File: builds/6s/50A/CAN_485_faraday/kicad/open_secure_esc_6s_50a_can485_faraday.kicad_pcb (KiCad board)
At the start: 4 copper layers, 32 x 66.1 mm, 59 parts, among them J1 SolderPad_1x04_SMD_P1.27mm_Pr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, J2 SolderPad_1x02_SMD_P2.54mm, J3 SolderPad_1x02_SMD_P2.54mm, J4A SolderWirePad_1x01_SMD_5x10mm, J4B SolderWirePad_1x01_SMD_5x10mm, J4C SolderWirePad_1x01_SMD_5x10mm, J5A SolderWire-6sqmm_1x01_D3.5mm_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, J5B SolderWire-6sqmm_1x01_D3.5mm_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, Q1 Toshiba_2-5W1A_SOP-Advance-N_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, Q2 Toshiba_2-5W1A_SOP-Advance-N_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, Q3 Toshiba_2-5W1A_SOP-Advance-N_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, Q4 Toshiba_2-5W1A_SOP-Advance-N_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, Q5 Toshiba_2-5W1A_SOP-Advance-N_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, Q6 Toshiba_2-5W1A_SOP-Advance-N_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, U1 LQFP-64_10x10mm_P0.5mm, U2 Infineon_PG-USON-10-2-4_3x3mm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, U3 SOIC-20W_7.5x12.8mm_P1.27mm, U4 SOIC-20W_7.5x12.8mm_P1.27mm, U5 TI_RTA0040B_WQFN-40_6x6mm_P0.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, U6 SOIC-8_3.9x4.9mm_P1.27mm, U7 SOIC-8_3.9x4.9mm_P1.27mm, U8 SOIC-8_3.9x4.9mm_P1.27mm

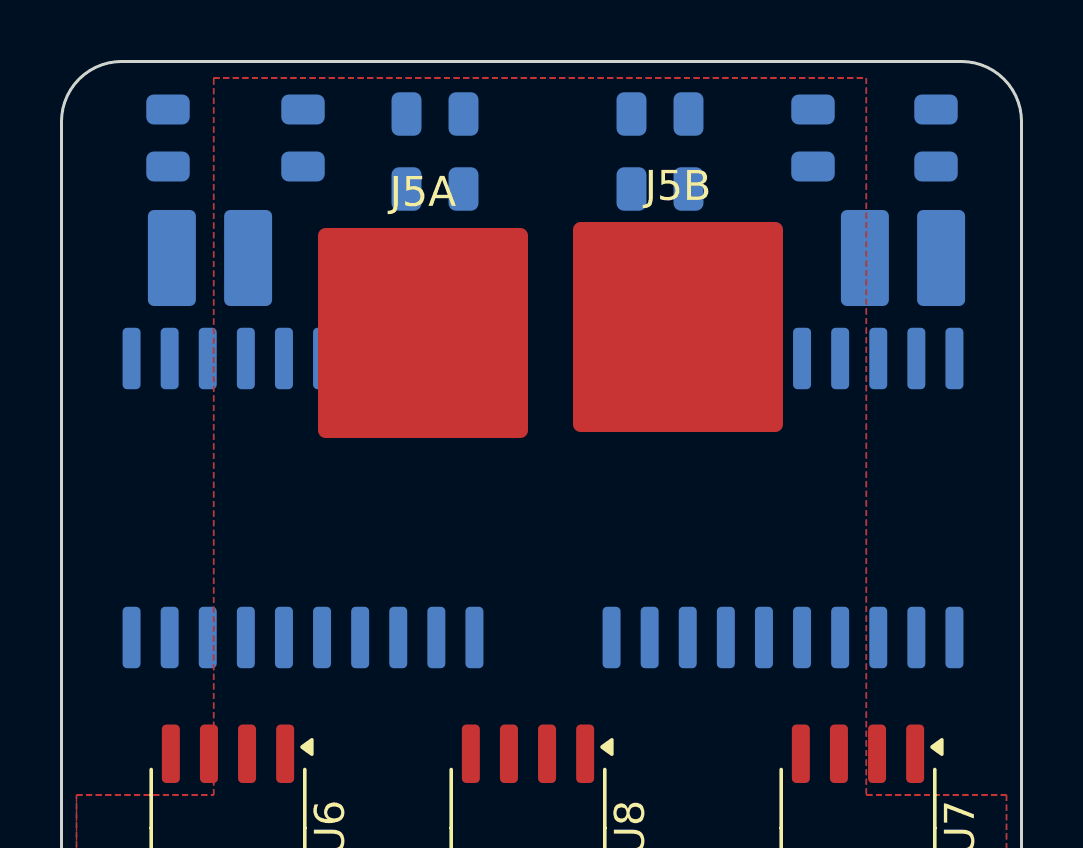
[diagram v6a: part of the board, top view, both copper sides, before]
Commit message: Score connectivity too: the +/-1.0 mm spread was breaking GND
Correcting the previous commit rather than leaving it standing. It applied a
+/-1.0 mm transceiver spread and reported "DRC electrical 0". The DRC number
was real; the conclusion drawn from it was not.

score_placement.py read only kicad-cli's "violations" array. kicad-cli reports
broken connections in a SEPARATE "unconnected_items" array, so the harness was
structurally blind to them. Checking by hand:

    before the spread   159 unconnected
    after  the spread   161 unconnected

The +/-1.0 mm move severed two GND connections. Refilling the pour around the
displaced parts fragments the B.Cu GND pour, and two of the eight newly
unconnected items belong to U5 -- a part that never moved. Gaining creepage by
cutting a ground connection is not a gain.

Re-swept with connectivity scored:

    spread   creepage   DRC-el   unconnected
    +/-0.00    7.51        0         159
    +/-0.25    7.66        0         159
    +/-0.50    7.83        0         159   <- applied
    +/-0.75    7.98        0         160
    +/-1.00    7.98        0         161

Backed off to +/-0.5 mm: creepage 7.51 -> 7.83 (0.33 mm margin, not the 0.48
previously claimed), isolated lead unchanged at 9.76 mm, both isolation rules
still passing, and no net broken. The extra 0.15 mm is available later if GND
stitching is done deliberately.

drc_electrical() now returns (violations, unconnected) and the report prints
the second with a BROKEN NETS marker. The 159 baseline is pre-existing and
largely unrouted copper, not damage from this work -- it is now visible on
every run instead of invisible on all of them.

Fourth harness defect found by checking output against geometry, and the first
one where the harness was not wrong about what it measured but silent about
what it did not.

Co-Authored-By: Claude Opus 5 <noreply@anthropic.com>
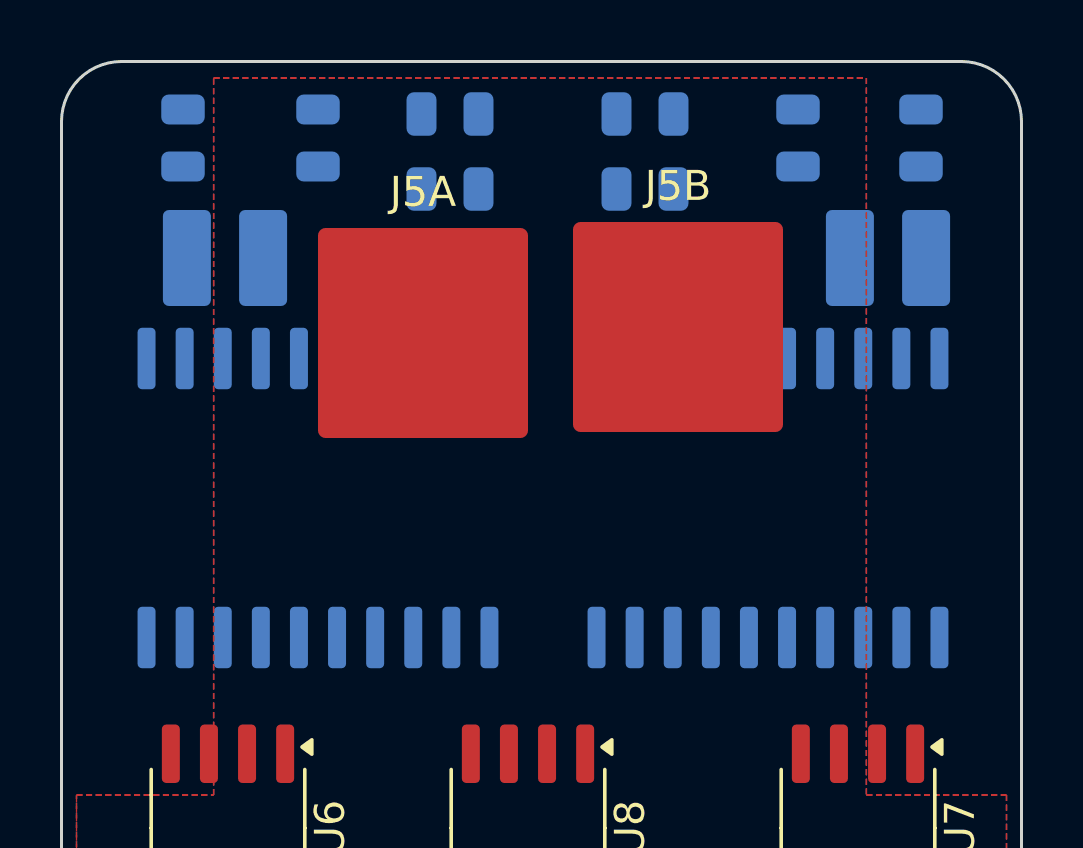
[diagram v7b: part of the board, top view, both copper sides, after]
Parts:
- moved C11 0.50 mm to (32.9, 21.7)
- moved C12 0.50 mm to (32.9, 24.2)
- moved C13 0.50 mm to (28.5, 22.5)
- moved C14 0.50 mm to (24.0, 22.5)
- moved C15 0.50 mm to (39.4, 21.7)
- moved C16 0.50 mm to (39.4, 24.2)
- moved C17 0.50 mm to (44.5, 22.5)
- moved C18 0.50 mm to (48.6, 22.5)
- moved FB1 0.50 mm to (32.4, 26.5)
- moved FB2 0.50 mm to (29.9, 26.5)
- moved FB3 0.50 mm to (39.4, 26.5)
- moved FB4 0.50 mm to (41.9, 26.5)
- moved J2 0.50 mm to (25.4, 26.5)
- moved J3 0.50 mm to (47.5, 26.5)
- moved U3 0.50 mm to (28.5, 34.5)
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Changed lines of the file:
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@@
 	(footprint "C_0805_2012Metric"
 		(layer "B.Cu")
-		(at 28 22.5 -90)
+		(at 28.5 22.5 -90)
 		(descr "Capacitor SMD 0805 (2012 Metric), square (rectangular) end terminal, IPC-7351 nominal, (Body size source: IPC-SM-782 page 76, https://www.pcb-3d.com/wordpress/wp-content/uploads/ipc-sm-782a_amendment_1_and_2.pdf, https://docs.google.com/spreadsheets/d/1BsfQQcO9C6DZCsRaXUlFlo91Tg2WpOkGARC1WS5S8t0/edit?usp=sharing), generated with kicad-footprint-generator")
 		(tags "capacitor")
@@
 	(footprint "C_0805_2012Metric"
 		(layer "B.Cu")
-		(at 32.4 21.7)
+		(at 32.9 21.7)
 		(descr "Capacitor SMD 0805 (2012 Metric), square (rectangular) end terminal, IPC-7351 nominal, (Body size source: IPC-SM-782 page 76, https://www.pcb-3d.com/wordpress/wp-content/uploads/ipc-sm-782a_amendment_1_and_2.pdf, https://docs.google.com/spreadsheets/d/1BsfQQcO9C6DZCsRaXUlFlo91Tg2WpOkGARC1WS5S8t0/edit?usp=sharing), generated with kicad-footprint-generator")
 		(tags "capacitor")
@@
 	(footprint "L_0402_1005Metric"
 		(layer "B.Cu")
-		(at 39.9 26.5)
+		(at 39.4 26.5)
 		(descr "Inductor SMD 0402 (1005 Metric), square (rectangular) end terminal, IPC-7351 nominal, (Body size source: http://www.tortai-tech.com/upload/download/2011102023233369053.pdf), generated with kicad-footprint-generator")
 		(tags "inductor")
@@
 	(footprint "SolderPad_1x02_SMD_P2.54mm"
 		(layer "B.Cu")
-		(at 24.9 26.5)
+		(at 25.4 26.5)
 		(descr "Bare SMD solder-pad strip, 2 pads, 2.54 mm pitch, 1.6 x 3.2 mm pads. Replaces a through-hole pin header so the opposite board side stays usable -- see symbols/tools/gen_smd_solder_pad_footprints.py. No connector body, no retention, no mating part: a wire solders directly to the pad. Pad geometry is an ENGINEERING DEFAULT (AGENTS.md Sec.4), not a datasheet or IPC value. Precedent: Vimdrones ESC S50 [47] 'CAN Port Connector: Solder PAD'.")
 		(tags "solder pad SMD wire connector 1x02 2.54mm")
@@
 	(footprint "SOIC-20W_7.5x12.8mm_P1.27mm"
 		(layer "B.Cu")
-		(at 44 34.5 90)
+		(at 43.5 34.5 90)
 		(descr "SOIC, 20 Pin (JEDEC MS-013AC, https://www.analog.com/media/en/package-pcb-resources/package/233848rw_20.pdf), generated with kicad-footprint-generator ipc_gullwing_generator.py")
 		(tags "SOIC SO")
@@
 	(footprint "C_0805_2012Metric"
 		(layer "B.Cu")
-		(at 39.9 21.7)
+		(at 39.4 21.7)
 		(descr "Capacitor SMD 0805 (2012 Metric), square (rectangular) end terminal, IPC-7351 nominal, (Body size source: IPC-SM-782 page 76, https://www.pcb-3d.com/wordpress/wp-content/uploads/ipc-sm-782a_amendment_1_and_2.pdf, https://docs.google.com/spreadsheets/d/1BsfQQcO9C6DZCsRaXUlFlo91Tg2WpOkGARC1WS5S8t0/edit?usp=sharing), generated with kicad-footprint-generator")
 		(tags "capacitor")
@@
 	(footprint "SOIC-20W_7.5x12.8mm_P1.27mm"
 		(layer "B.Cu")
-		(at 28 34.5 90)
+		(at 28.5 34.5 90)
 		(descr "SOIC, 20 Pin (JEDEC MS-013AC, https://www.analog.com/media/en/package-pcb-resources/package/233848rw_20.pdf), generated with kicad-footprint-generator ipc_gullwing_generator.py")
 		(tags "SOIC SO")
@@
 	(footprint "C_0805_2012Metric"
 		(layer "B.Cu")
-		(at 45 22.5 -90)
+		(at 44.5 22.5 -90)
 		(descr "Capacitor SMD 0805 (2012 Metric), square (rectangular) end terminal, IPC-7351 nominal, (Body size source: IPC-SM-782 page 76, https://www.pcb-3d.com/wordpress/wp-content/uploads/ipc-sm-782a_amendment_1_and_2.pdf, https://docs.google.com/spreadsheets/d/1BsfQQcO9C6DZCsRaXUlFlo91Tg2WpOkGARC1WS5S8t0/edit?usp=sharing), generated with kicad-footprint-generator")
 		(tags "capacitor")
@@
 	(footprint "L_0402_1005Metric"
 		(layer "B.Cu")
-		(at 29.4 26.5)
+		(at 29.9 26.5)
 		(descr "Inductor SMD 0402 (1005 Metric), square (rectangular) end terminal, IPC-7351 nominal, (Body size source: http://www.tortai-tech.com/upload/download/2011102023233369053.pdf), generated with kicad-footprint-generator")
 		(tags "inductor")
@@
 	(footprint "C_0805_2012Metric"
 		(layer "B.Cu")
-		(at 32.4 24.2)
+		(at 32.9 24.2)
 		(descr "Capacitor SMD 0805 (2012 Metric), square (rectangular) end terminal, IPC-7351 nominal, (Body size source: IPC-SM-782 page 76, https://www.pcb-3d.com/wordpress/wp-content/uploads/ipc-sm-782a_amendment_1_and_2.pdf, https://docs.google.com/spreadsheets/d/1BsfQQcO9C6DZCsRaXUlFlo91Tg2WpOkGARC1WS5S8t0/edit?usp=sharing), generated with kicad-footprint-generator")
 		(tags "capacitor")
@@
 	(footprint "L_0402_1005Metric"
 		(layer "B.Cu")
-		(at 42.4 26.5)
+		(at 41.9 26.5)
 		(descr "Inductor SMD 0402 (1005 Metric), square (rectangular) end terminal, IPC-7351 nominal, (Body size source: http://www.tortai-tech.com/upload/download/2011102023233369053.pdf), generated with kicad-footprint-generator")
 		(tags "inductor")
@@
 	(footprint "C_0805_2012Metric"
 		(layer "B.Cu")
-		(at 23.5 22.5 -90)
+		(at 24 22.5 -90)
 		(descr "Capacitor SMD 0805 (2012 Metric), square (rectangular) end terminal, IPC-7351 nominal, (Body size source: IPC-SM-782 page 76, https://www.pcb-3d.com/wordpress/wp-content/uploads/ipc-sm-782a_amendment_1_and_2.pdf, https://docs.google.com/spreadsheets/d/1BsfQQcO9C6DZCsRaXUlFlo91Tg2WpOkGARC1WS5S8t0/edit?usp=sharing), generated with kicad-footprint-generator")
 		(tags "capacitor")
@@
 	(footprint "L_0402_1005Metric"
 		(layer "B.Cu")
-		(at 31.9 26.5)
+		(at 32.4 26.5)
 		(descr "Inductor SMD 0402 (1005 Metric), square (rectangular) end terminal, IPC-7351 nominal, (Body size source: http://www.tortai-tech.com/upload/download/2011102023233369053.pdf), generated with kicad-footprint-generator")
 		(tags "inductor")
@@
 	(footprint "SolderPad_1x02_SMD_P2.54mm"
 		(layer "B.Cu")
-		(at 48 26.5)
+		(at 47.5 26.5)
 		(descr "Bare SMD solder-pad strip, 2 pads, 2.54 mm pitch, 1.6 x 3.2 mm pads. Replaces a through-hole pin header so the opposite board side stays usable -- see symbols/tools/gen_smd_solder_pad_footprints.py. No connector body, no retention, no mating part: a wire solders directly to the pad. Pad geometry is an ENGINEERING DEFAULT (AGENTS.md Sec.4), not a datasheet or IPC value. Precedent: Vimdrones ESC S50 [47] 'CAN Port Connector: Solder PAD'.")
 		(tags "solder pad SMD wire connector 1x02 2.54mm")
@@
 	(footprint "C_0805_2012Metric"
 		(layer "B.Cu")
-		(at 39.9 24.2)
+		(at 39.4 24.2)
 		(descr "Capacitor SMD 0805 (2012 Metric), square (rectangular) end terminal, IPC-7351 nominal, (Body size source: IPC-SM-782 page 76, https://www.pcb-3d.com/wordpress/wp-content/uploads/ipc-sm-782a_amendment_1_and_2.pdf, https://docs.google.com/spreadsheets/d/1BsfQQcO9C6DZCsRaXUlFlo91Tg2WpOkGARC1WS5S8t0/edit?usp=sharing), generated with kicad-footprint-generator")
 		(tags "capacitor")
@@
 	(footprint "C_0805_2012Metric"
 		(layer "B.Cu")
-		(at 49.1 22.5 -90)
+		(at 48.6 22.5 -90)
 		(descr "Capacitor SMD 0805 (2012 Metric), square (rectangular) end terminal, IPC-7351 nominal, (Body size source: IPC-SM-782 page 76, https://www.pcb-3d.com/wordpress/wp-content/uploads/ipc-sm-782a_amendment_1_and_2.pdf, https://docs.google.com/spreadsheets/d/1BsfQQcO9C6DZCsRaXUlFlo91Tg2WpOkGARC1WS5S8t0/edit?usp=sharing), generated with kicad-footprint-generator")
 		(tags "capacitor")

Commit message: Clean build pass: 78 -> 16 DRC violations, zero errors remaining
The courtyard problem I reported turned out not to exist, so this addresses
the violations the board actually has. Every error-severity violation is now
resolved; all 16 remaining are warnings.

    drill_out_of_range   12 -> 0    (error)
    starved_thermal      11 -> 0    (error)
    isolated_copper       2 -> 1    (warning)
    silk_over_copper     35 -> 8    (warning)
    silk_overlap         18 -> 7    (warning)
    unconnected         159 -> 158

Creepage holds at 7.83 mm, both isolation rules still PASS, DRC electrical 0.

tools/fix_u5_thermal_vias.py
  U5's 12 GND thermal vias 0.400/0.200 -> 0.600/0.300 mm. Not a chosen
  number: that is the Default net class via already in .kicad_pro, so every
  constraint is satisfied by construction (annular 0.150 vs 0.100 min,
  hole-to-hole 0.85 vs 0.25 min). This board has produced one verified
  GND-to-VM short from the U5-under-FETs stack-up, so the drain lands were
  measured before growing copper on every layer: the array sits in the ~6 mm
  gap between Q3 and Q4, 0.725 mm clear at the new radius.

tools/fix_starved_thermals.py
  11 GND pads were hanging off the pour by a single 0.5 mm spoke against a
  min_resolved_spokes = 2 rule. Set solid. A spoke cannot be conjured where
  the pour does not reach. It is also correct for a board whose entire
  premise is EMI survival -- a Faraday shield bonded through one narrow neck
  is mostly inductance. The reflow trade is real and split out: the 9
  IC/shield pads are low risk, the 5 two-terminal 0805 passives are the
  tombstoning case, and --skip-passives reverts exactly those.

tools/remove_vm_island.py
  A 4.313 mm^2 VM pocket on In2.Cu, fenced inside U5's via ring with nothing
  on net VM in it -- a floating plate under a switching gate driver. Excluded
  with a scoped In2.Cu rule area. island_removal_mode was already ALWAYS and
  did not remove it; a clean reload-fill-save reproduced it, so not the
  st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
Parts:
- moved J5B 0.20 mm to (40.5, 29.0)
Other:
- board text added: "Open Secure ESC 50A 6S Shielded CAN + RS485 Griffing Tech LLC CERN-OHL-P 2.0 2026"
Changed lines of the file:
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@@
 			(roundrect_rratio 0.25)
 			(net 8 "GND")
+			(zone_connect 2)
 		)
 		(pad "2" smd roundrect
@@
 			(roundrect_rratio 0.25)
 			(net 8 "GND")
+			(zone_connect 2)
 		)
 		(pad "3" smd roundrect
@@
 	(footprint "SolderWire-6sqmm_1x01_D3.5mm_OD7mm"
 		(layer "F.Cu")
-		(at 40.5 28.8)
+		(at 40.5 29)
 		(descr "Soldered wire connection, for a single 6 mm² wire, reinforced insulation, conductor diameter 3.5mm, outer diameter 7mm, size source Multi-Contact FLEXI-xV 2.5 (https://www.staubli.com/content/dam/ecs/catalogs-brochures/TM/CAB-Main-11014119-en.pdf#page=11), bend radius 3 times outer diameter, generated with kicad-footprint-generator")
 		(tags "connector wire 6sqmm")
@@
 			(roundrect_rratio 0.25)
 			(net 8 "GND")
+			(zone_connect 2)
 		)
 		(pad "2" smd roundrect
@@
 			(roundrect_rratio 0.25)
 			(net 8 "GND")
+			(zone_connect 2)
 		)
 		(pad "3" smd roundrect
@@
 			(roundrect_rratio 0.25)
 			(net 8 "GND")
+			(zone_connect 2)
 		)
 		(embedded_fonts no)
@@
 			(roundrect_rratio 0.243902)
 			(net 8 "GND")
+			(zone_connect 2)
 		)
 		(embedded_fonts no)
@@
 			(roundrect_rratio 0.243902)
 			(net 8 "GND")
+			(zone_connect 2)
 		)
 		(embedded_fonts no)
@@
 			(roundrect_rratio 0.25)
 			(net 8 "GND")
+			(zone_connect 2)
 		)
 		(embedded_fonts no)
@@
 			(roundrect_rratio 0.25)
 			(net 8 "GND")
+			(zone_connect 2)
 		)
 		(embedded_fonts no)
@@
 			(roundrect_rratio 0.227273)
 			(net 8 "GND")
+			(zone_connect 2)
 		)
 		(pad "26" smd roundrect
@@
 		(pad "41" thru_hole circle
 			(at -1.725 -1.725 180)
-			(size 0.4 0.4)
-			(drill 0.2)
+			(size 0.6 0.6)
+			(drill 0.3)
 			(layers "*.Cu" "*.Mask")
 			(remove_unused_layers no)
@@
 		(pad "41" thru_hole circle
 			(at -1.725 -0.575 180)
-			(size 0.4 0.4)
-			(drill 0.2)
+			(size 0.6 0.6)
+			(drill 0.3)
 			(layers "*.Cu" "*.Mask")
 			(remove_unused_layers no)
@@
 		(pad "41" thru_hole circle
 			(at -1.725 0.575 180)
-			(size 0.4 0.4)
-			(drill 0.2)
+			(size 0.6 0.6)
+			(drill 0.3)
 			(layers "*.Cu" "*.Mask")
 			(remove_unused_layers no)
@@
 		(pad "41" thru_hole circle
 			(at -1.725 1.725 180)
-			(size 0.4 0.4)
-			(drill 0.2)
+			(size 0.6 0.6)
+			(drill 0.3)
 			(layers "*.Cu" "*.Mask")
 			(remove_unused_layers no)
@@
 		(pad "41" thru_hole circle
 			(at -0.575 -1.725 180)
-			(size 0.4 0.4)
-			(drill 0.2)
+			(size 0.6 0.6)
+			(drill 0.3)
 			(layers "*.Cu" "*.Mask")
 			(remove_unused_layers no)
@@
 		(pad "41" thru_hole circle
 			(at -0.575 1.725 180)
-			(size 0.4 0.4)
-			(drill 0.2)
+			(size 0.6 0.6)
+			(drill 0.3)
 			(layers "*.Cu" "*.Mask")
 			(remove_unused_layers no)
@@
 		(pad "41" thru_hole circle
 			(at 0.575 -1.725 180)
-			(size 0.4 0.4)
-			(drill 0.2)
+			(size 0.6 0.6)
+			(drill 0.3)
 			(layers "*.Cu" "*.Mask")
 			(remove_unused_layers no)
@@
 		(pad "41" thru_hole circle
 			(at 0.575 1.725 180)
-			(size 0.4 0.4)
-			(drill 0.2)
+			(size 0.6 0.6)
+			(drill 0.3)
 			(layers "*.Cu" "*.Mask")
 			(remove_unused_layers no)
@@
 		(pad "41" thru_hole circle
 			(at 1.725 -1.725 180)
-			(size 0.4 0.4)
-			(drill 0.2)
+			(size 0.6 0.6)
+			(drill 0.3)
 			(layers "*.Cu" "*.Mask")
 			(remove_unused_layers no)
@@
 		(pad "41" thru_hole circle
 			(at 1.725 -0.575 180)
-			(size 0.4 0.4)
-			(drill 0.2)
+			(size 0.6 0.6)
+			(drill 0.3)
 			(layers "*.Cu" "*.Mask")
 			(remove_unused_layers no)
@@
 		(pad "41" thru_hole circle
 			(at 1.725 0.575 180)
-			(size 0.4 0.4)
-			(drill 0.2)
+			(size 0.6 0.6)
+			(drill 0.3)
 			(layers "*.Cu" "*.Mask")
 			(remove_unused_layers no)
@@
 		(pad "41" thru_hole circle
 			(at 1.725 1.725 180)
-			(size 0.4 0.4)
-			(drill 0.2)
+			(size 0.6 0.6)
+			(drill 0.3)
 			(layers "*.Cu" "*.Mask")
 			(remove_unused_layers no)
@@
 			(layers "B.Cu" "B.Mask")
 			(net 8 "GND")
+			(zone_connect 2)
 		)
 		(pad "1" smd rect
@@
 			(layers "B.Cu" "B.Mask")
 			(net 8 "GND")
+			(zone_connect 2)
 		)
 		(pad "1" smd rect
@@
 			(layers "B.Cu" "B.Mask")
 			(net 8 "GND")
+			(zone_connect 2)
 		)
 		(pad "1" smd rect
@@
 			(layers "B.Cu" "B.Mask")
 			(net 8 "GND")
+			(zone_connect 2)
 		)
 		(embedded_fonts no)
@@
 		(layer "Edge.Cuts")
 	)
+	(gr_text "Open Secure ESC\n50A 6S Shielded CAN + RS485\nGriffing Tech LLC \nCERN-OHL-P 2.0  2026\n"
+		(at 36.5 40 0)
+		(layer "F.SilkS")
+		(effects
+			(font
+				(size 1 1)
+				(thickness 0.2)
+				(bold yes)
+			)
+			(justify bottom)
+		)
+	)
 	(zone
